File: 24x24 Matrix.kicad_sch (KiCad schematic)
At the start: 23 parts, among them J1 Conn_01x06_Pin, J2 Conn_01x06_Pin, J3 SM06B-GHS-TB

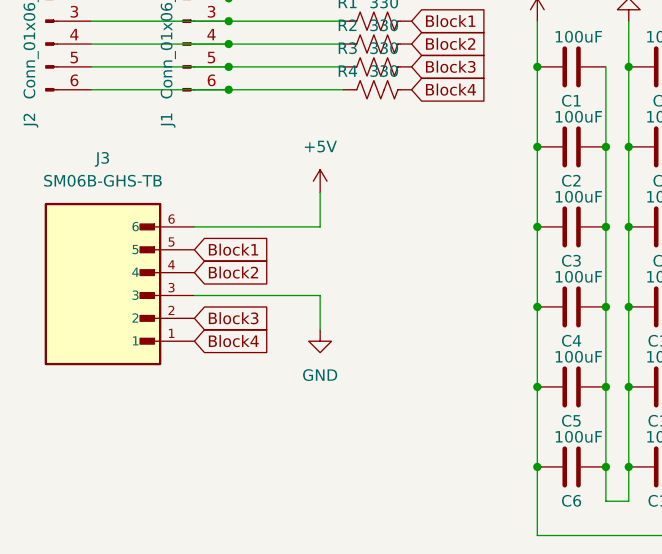
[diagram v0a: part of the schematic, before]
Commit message: Added silkscreen and changed connector wiring
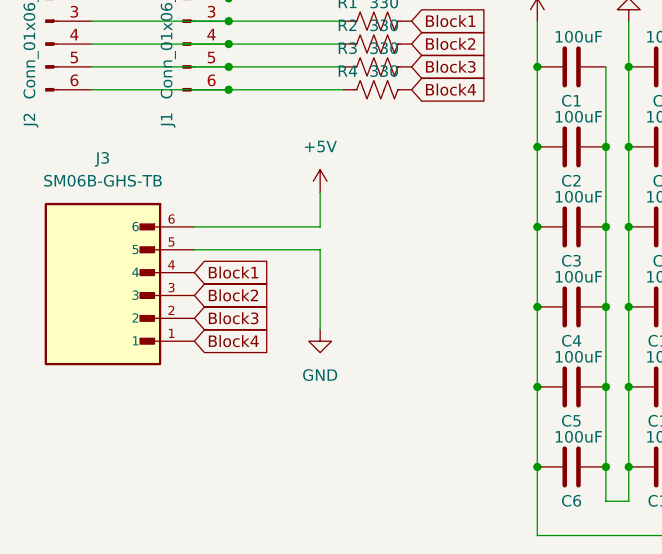
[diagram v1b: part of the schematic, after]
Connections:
- net Block1: now also J3.4; no longer J3.5
- net Block2: now also J3.3; no longer J3.4
- net GND: now also J3.5; no longer J3.3
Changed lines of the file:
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@@
 	(wire
 		(pts
-			(xy 121.92 298.45) (xy 121.92 302.26)
+			(xy 121.92 293.37) (xy 121.92 302.26)
 		)
 		(stroke
@@
 	(wire
 		(pts
+			(xy 121.92 293.37) (xy 107.95 293.37)
+		)
+		(stroke
+			(width 0)
+			(type default)
+		)
+	)
+	(wire
+		(pts
 			(xy 165.1 254) (xy 165.1 259.08)
 		)
@@
 		(pts
 			(xy 153.67 299.72) (xy 153.67 308.61)
-		)
-		(stroke
-			(width 0)
-			(type default)
-		)
-	)
-	(wire
-		(pts
-			(xy 107.95 298.45) (xy 121.92 298.45)
 		)
 		(stroke
@@
 	(global_label "Block2"
 		(shape input)
-		(at 107.95 295.91 0)
-		(fields_autoplaced yes)
-		(effects
-			(font
-				(size 1.27 1.27)
-			)
-			(justify left)
-		)
-		(property "Intersheetrefs" "${INTERSHEET_REFS}"
-			(at 117.3456 295.91 0)
+		(at 107.95 298.45 0)
+		(fields_autoplaced yes)
+		(effects
+			(font
+				(size 1.27 1.27)
+			)
+			(justify left)
+		)
+		(property "Intersheetrefs" "${INTERSHEET_REFS}"
+			(at 117.3456 298.45 0)
 			(hide yes)
 			(show_name no)
@@
 	(global_label "Block1"
 		(shape input)
-		(at 107.95 293.37 0)
-		(fields_autoplaced yes)
-		(effects
-			(font
-				(size 1.27 1.27)
-			)
-			(justify left)
-		)
-		(property "Intersheetrefs" "${INTERSHEET_REFS}"
-			(at 117.3456 293.37 0)
-			(hide yes)
-			(show_name no)
+		(at 107.95 295.91 0)
+		(fields_autoplaced yes)
+		(effects
+			(font
+				(size 1.27 1.27)
+			)
+			(justify left)
+		)
+		(property "Intersheetrefs" "${INTERSHEET_REFS}"
+			(at 117.3456 295.91 0)
+			(hide yes)
+			(show_name no)
